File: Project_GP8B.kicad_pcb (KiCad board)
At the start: 4 copper layers, 133 x 93 mm, 96 parts, among them IC1 XC95288XL-10TQ144I, J1 Conn_01x05_Male, J2 TE_Eurocard_96pole, J3 5530843-2, J4 Conn_02x21_Odd_Even, U1 74AHC05, U10 74AHC1G04, U11 CD74AC238, U12 74AHC1G04, U13 CD74AC238, U14 74AHC08, U15 CD74AC238, U16 74AHC08, U17 74AHC138, U18 74HC165, U19 74AHCT244, U2 74AHC05, U20 74AHCT244, U21 74AHCT244, U22 74AHCT244, U23 74AHCT244, U24 74AHC273, U25 74AHCT595, U26 74AHC273, U27 74AHC273, U29 74AHC273, U3 74AHC1G04, U31 74AHC273, U33 74AHC273, U35 74AHC273, U36 74AHC1G04, U37 74AHC273, U38 74AHC374, U39 74AHC1G04, U4 74AHC1G04, U5 74AHC05, U6 74AHC273, U7 74AHCT273, U8 74HC163, U9 CD74AC238

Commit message: Adding license info on silks
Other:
- board text added: "Licensed under CERN OHL v.1.2"
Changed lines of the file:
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@@
   (general
     (thickness 1.6)
-    (drawings 29)
+    (drawings 30)
     (tracks 4985)
     (zones 0)
@@
     )
   )
+  (gr_text "Licensed under CERN OHL v.1.2" (at 170.3 122) (layer F.SilkS)
+    (effects (font (size 1 1) (thickness 0.15)))
+  )
   (gr_text "ALU - Unused pins" (at 108.5 114.5) (layer F.SilkS)

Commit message: Switching license to "CERN-OHLw v2 or later"
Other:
- board text added: "Licensed under CERN-OHL-W v2 or later"
- board text removed: "Licensed under CERN OHL v.1.2"

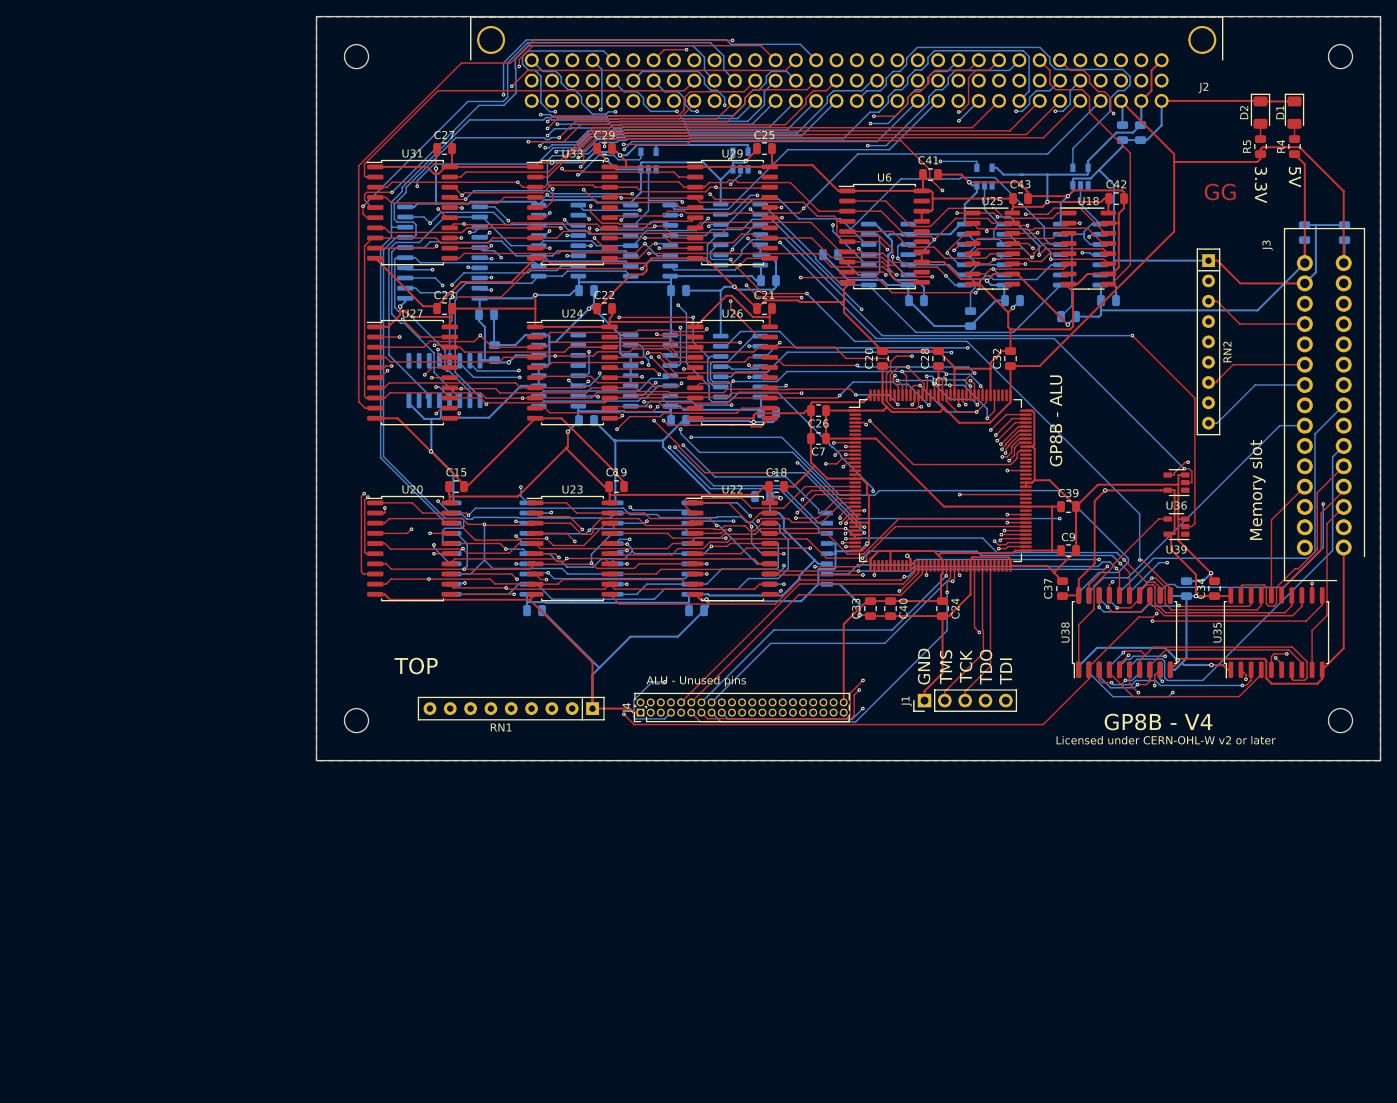
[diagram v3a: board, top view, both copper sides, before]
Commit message: Preparing footprint placement, removing old footprint
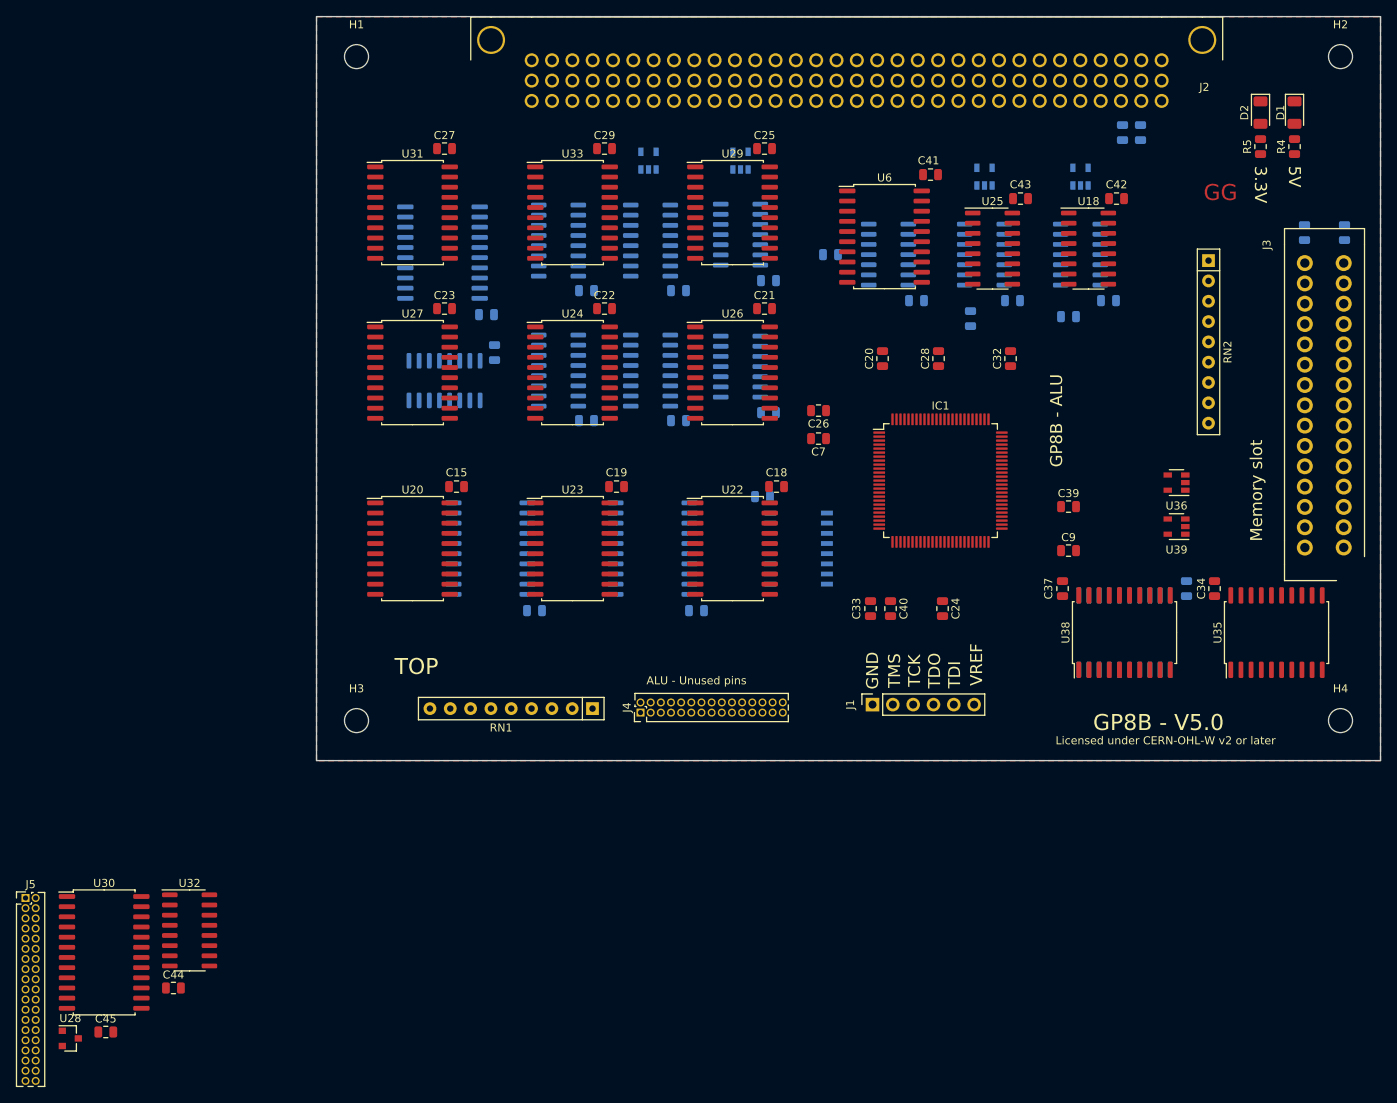
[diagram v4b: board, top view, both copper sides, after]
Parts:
- removed HOLE1, HOLE2, HOLE3, HOLE4: Hole_3mm, hole_3mm:Hole_3mm
- added C44: 10nF, Capacitor_SMD:C_0805_2012Metric, F.Cu at (43.1, 152.9)
- added C45: 10nF, Capacitor_SMD:C_0805_2012Metric, F.Cu at (34.7, 158.4)
- added H1: MountingHole_3mm, MountingHole:MountingHole_3mm, F.Cu at (66.0, 36.5)
- added H2: MountingHole_3mm, MountingHole:MountingHole_3mm, F.Cu at (189.0, 36.5)
- added H3: MountingHole_3mm, MountingHole:MountingHole_3mm, F.Cu at (66.0, 119.5)
- added H4: MountingHole_3mm, MountingHole:MountingHole_3mm, F.Cu at (189.0, 119.5)
- added J5: ALU_PINS, Connector_PinHeader_1.27mm:PinHeader_2x19_P1.27mm_Vertical, F.Cu at (24.6, 141.7)
- added U28: TPS7A0518PDBZR, Package_TO_SOT_SMD:SOT-23, F.Cu at (30.2, 159.2)
- added U30: SN74LVC8T245DW, Package_SO:SOIC-24W_7.5x15.4mm_P1.27mm, F.Cu at (34.5, 148.5)
- added U32: SN74AVC4T245D, Package_SO:SOIC-16_3.9x9.9mm_P1.27mm, F.Cu at (45.1, 145.7)
- C20, C24, C26, C28, C32, C39, C7, C9: value 10nF -> 100nF
- C33, C40: value 10nF -> 1uF
- IC1: value XC95288XL-10TQ144I -> XC2C256-VQ100; footprint Package_QFP:TQFP-144_20x20mm_P0.5mm -> Package_QFP:VQFP-100_14x14mm_P0.5mm
- J1: value Conn_01x05_Male -> ALU_JTAG; footprint Connector_PinHeader_2.54mm:PinHeader_1x05_P2.54mm_Vertical -> Connector_PinSocket_2.54mm:PinSocket_1x06_P2.54mm_Vertical
- J4: value Conn_02x21_Odd_Even -> UnusedPins_Connector; footprint Connector_PinHeader_1.27mm:PinHeader_2x21_P1.27mm_Vertical -> Connector_PinHeader_1.27mm:PinHeader_2x15_P1.27mm_Vertical
- moved J1 6.52 mm to (130.5, 117.5)
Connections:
- net /BCSPI_CLK renamed /BCFG_SPI_CLK
- net /Connecteur/BDATASRC_0 renamed /Connector/BDATASRC_0
- net /Connecteur/BDATASRC_1 renamed /Connector/BDATASRC_1
- net /Connecteur/BDATASRC_2 renamed /Connector/BDATASRC_2
- net /Connecteur/BDATASRC_3 renamed /Connector/BDATASRC_3
- net /Connecteur/BDATASRC_4 renamed /Connector/BDATASRC_4
- net /Connecteur/BDATASRC_5 renamed /Connector/BDATASRC_5
- net /Connecteur/BDATASRC_6 renamed /Connector/BDATASRC_6
- net /Connecteur/BDATASRC_7 renamed /Connector/BDATASRC_7
- net /Connecteur/BJMPSRC_0 renamed /Connector/BJMPSRC_0
- net /Connecteur/BJMPSRC_1 renamed /Connector/BJMPSRC_1
- net /Connecteur/BJMPSRC_10 renamed /Connector/BJMPSRC_10
- net /Connecteur/BJMPSRC_11 renamed /Connector/BJMPSRC_11
- net /Connecteur/BJMPSRC_12 renamed /Connector/BJMPSRC_12
- net /Connecteur/BJMPSRC_13 renamed /Connector/BJMPSRC_13
- net /Connecteur/BJMPSRC_14 renamed /Connector/BJMPSRC_14
- net /Connecteur/BJMPSRC_15 renamed /Connector/BJMPSRC_15
- net /Connecteur/BJMPSRC_16 renamed /Connector/BJMPSRC_16
- net /Connecteur/BJMPSRC_17 renamed /Connector/BJMPSRC_17
- net /Connecteur/BJMPSRC_18 renamed /Connector/BJMPSRC_18
- net /Connecteur/BJMPSRC_19 renamed /Connector/BJMPSRC_19
- net /Connecteur/BJMPSRC_2 renamed /Connector/BJMPSRC_2
- net /Connecteur/BJMPSRC_20 renamed /Connector/BJMPSRC_20
- net /Connecteur/BJMPSRC_21 renamed /Connector/BJMPSRC_21
- net /Connecteur/BJMPSRC_22 renamed /Connector/BJMPSRC_22
- net /Connecteur/BJMPSRC_23 renamed /Connector/BJMPSRC_23
- net /Connecteur/BJMPSRC_3 renamed /Connector/BJMPSRC_3
- net /Connecteur/BJMPSRC_4 renamed /Connector/BJMPSRC_4
- net /Connecteur/BJMPSRC_5 renamed /Connector/BJMPSRC_5
- net /Connecteur/BJMPSRC_6 renamed /Connector/BJMPSRC_6
- net /Connecteur/BJMPSRC_7 renamed /Connector/BJMPSRC_7
- net /Connecteur/BJMPSRC_8 renamed /Connector/BJMPSRC_8
- net /Connecteur/BJMPSRC_9 renamed /Connector/BJMPSRC_9
- net /Connecteur/BPCS_0 renamed /Connector/BPCS_0
- net /Connecteur/BPCS_1 renamed /Connector/BPCS_1
- net /Connecteur/BPCS_2 renamed /Connector/BPCS_2
- net /Connecteur/BPCS_3 renamed /Connector/BPCS_3
- net /Connecteur/BPCS_4 renamed /Connector/BPCS_4
- net /Connecteur/BPCS_5 renamed /Connector/BPCS_5
- net /Connecteur/BREAD1_0 renamed /Connector/BREAD1_0
- net /Connecteur/BREAD1_1 renamed /Connector/BREAD1_1
- net /Connecteur/BREAD1_2 renamed /Connector/BREAD1_2
- net /Connecteur/BREAD1_3 renamed /Connector/BREAD1_3
- net /Connecteur/BREAD1_4 renamed /Connector/BREAD1_4
- net /Connecteur/BREAD1_5 renamed /Connector/BREAD1_5
- net /Connecteur/BREAD1_6 renamed /Connector/BREAD1_6
- net /Connecteur/BREAD1_7 renamed /Connector/BREAD1_7
- net /Connecteur/BREAD2_0 renamed /Connector/BREAD2_0
- net /Connecteur/BREAD2_1 renamed /Connector/BREAD2_1
- net /Connecteur/BREAD2_2 renamed /Connector/BREAD2_2
- net /Connecteur/BREAD2_3 renamed /Connector/BREAD2_3
- net /Connecteur/BREAD2_4 renamed /Connector/BREAD2_4
- net /Connecteur/BREAD2_5 renamed /Connector/BREAD2_5
- net /Connecteur/BREAD2_6 renamed /Connector/BREAD2_6
- net /Connecteur/BREAD2_7 renamed /Connector/BREAD2_7
- net /Connecteur/BWRITE1_0 renamed /Connector/BWRITE1_0
- net /Connecteur/BWRITE1_1 renamed /Connector/BWRITE1_1
- net /Connecteur/BWRITE1_2 renamed /Connector/BWRITE1_2
- net /Connecteur/BWRITE1_3 renamed /Connector/BWRITE1_3
- net /Connecteur/BWRITE1_4 renamed /Connector/BWRITE1_4
- net /Connecteur/BWRITE1_5 renamed /Connector/BWRITE1_5
- net /Connecteur/BWRITE1_6 renamed /Connector/BWRITE1_6
- net /Connecteur/BWRITE1_7 renamed /Connector/BWRITE1_7
- net /Connecteur/BWRITE2_0 renamed /Connector/BWRITE2_0
- net /Connecteur/BWRITE2_1 renamed /Connector/BWRITE2_1
- net /Connecteur/BWRITE2_2 renamed /Connector/BWRITE2_2
- net /Connecteur/BWRITE2_3 renamed /Connector/BWRITE2_3
- net /Connecteur/BWRITE2_4 renamed /Connector/BWRITE2_4
- net /Connecteur/BWRITE2_5 renamed /Connector/BWRITE2_5
- net /Connecteur/BWRITE2_6 renamed /Connector/BWRITE2_6
- net /Connecteur/BWRITE2_7 renamed /Connector/BWRITE2_7
- C24 pad 1: +3V3 -> +1V8
- C28 pad 1: +3V3 -> +1V8
- C40 pad 1: +3V3 -> +1V8
- IC1 pad 1: +3V3 -> /NumberSelect/BOPRESULT_4
- IC1 pad 10: /Operation/UNUSED_A0 -> /Operation/DLEFT_4
- IC1 pad 100: /Operation/UNUSED_C7 -> GND
- IC1 pad 11: /Operation/UNUSED_A1 -> /Operation/DLEFT_5
- IC1 pad 12: /Operation/UNUSED_A2 -> /Operation/DLEFT_6
- IC1 pad 13: /Operation/UNUSED_A3 -> /Operation/DLEFT_7
- IC1 pad 14: /NumberSelect/BOPRESULT_5 -> Net-(IC1-Pad14)
- IC1 pad 18: GND -> Net-(IC1-Pad18)
- IC1 pad 19: Net-(IC1-Pad19) -> /NumberSelect/BOPRESULT_7
- IC1 pad 2: Net-(IC1-Pad2) -> /Operation/UNUSED_D2
- IC1 pad 20: /NumberSelect/BOPRESULT_0 -> +3V3
- IC1 pad 21: /Operation/UNUSED_A4 -> GND
- IC1 pad 22: /Operation/UNUSED_A5 -> /Operation/CPLD_OPCHOOSE_CLK
- IC1 pad 23: /Operation/UNUSED_A6 -> /Operation/CPLD_OPRIGHT_CLK
- IC1 pad 24: /Operation/UNUSED_A7 -> /NumberSelect/BOPRESULT_6
- IC1 pad 25: /Operation/UNUSED_E0 -> GND
- IC1 pad 26: /Operation/UNUSED_E1 -> +1V8
- IC1 pad 27: /Operation/UNUSED_E2 -> /Operation/CPLD_OPLEFT_CLK
- IC1 pad 28: /Operation/UNUSED_E3 -> /Operation/UNUSED_D3
- IC1 pad 29: GND -> /Operation/DLEFT_0
- IC1 pad 3: Net-(IC1-Pad3) -> /Operation/UNUSED_D1
- IC1 pad 30: /OPLEFT_CLK -> /Operation/DLEFT_1
- IC1 pad 31: /Operation/UNUSED_E4 -> GND
- IC1 pad 32: /OPRIGHT_CLK -> /Operation/DLEFT_2
- IC1 pad 33: /Operation/UNUSED_E5 -> /Operation/DLEFT_3
- IC1 pad 34: /Operation/UNUSED_E6 -> /Operation/DLEFT_4
- IC1 pad 35: /Operation/UNUSED_E7 -> /Operation/DLEFT_5
- IC1 pad 36: GND -> /Operation/DLEFT_6
- IC1 pad 37: +3V3 -> /Operation/DLEFT_7
- IC1 pad 38: /OPC_CLK -> +3V3
- IC1 pad 4: /NumberSelect/BOPRESULT_7 -> /Operation/UNUSED_D0
- IC1 pad 40: Net-(IC1-Pad40) -> /Operation/UNUSED_C0
- IC1 pad 41: Net-(IC1-Pad41) -> /Operation/UNUSED_C1
- IC1 pad 42: +3V3 -> /Operation/UNUSED_C2
- IC1 pad 43: Net-(IC1-Pad43) -> /Operation/UNUSED_C3
- IC1 pad 44: Net-(IC1-Pad44) -> /Operation/UNUSED_C4
- IC1 pad 45: Net-(IC1-Pad45) -> /Operation/TDI
- IC1 pad 46: Net-(IC1-Pad46) -> /Operation/UNUSED_C5
- IC1 pad 47: GND -> /Operation/TMS
- IC1 pad 48: /Operation/UNUSED_B0 -> /Operation/TCK
- IC1 pad 49: /Operation/UNUSED_B1 -> /Operation/UNUSED_C6
- IC1 pad 5: Net-(IC1-Pad5) -> +3V3
- IC1 pad 50: /Operation/UNUSED_B2 -> /Operation/UNUSED_C7
- IC1 pad 51: /Operation/UNUSED_B3 -> +3V3
- IC1 pad 52: Net-(IC1-Pad52) -> /Operation/UNUSED_A0
- IC1 pad 53: Net-(IC1-Pad53) -> /Operation/UNUSED_A1
- IC1 pad 54: Net-(IC1-Pad54) -> /Operation/UNUSED_A2
- IC1 pad 55: +3V3 -> /Operation/UNUSED_A3
- IC1 pad 56: /Operation/UNUSED_B4 -> /Operation/UNUSED_A4
- IC1 pad 57: /Operation/UNUSED_B5 -> +1V8
- IC1 pad 58: /Operation/UNUSED_B6 -> /Operation/UNUSED_A5
- IC1 pad 59: /Operation/UNUSED_B7 -> /Operation/UNUSED_A6
- IC1 pad 6: Net-(IC1-Pad6) -> /Operation/DLEFT_0
- IC1 pad 60: Net-(IC1-Pad60) -> /Operation/UNUSED_A7
- IC1 pad 63: /Operation/TDI -> Net-(IC1-Pad63)
- IC1 pad 65: /Operation/TMS -> Net-(IC1-Pad65)
- IC1 pad 66: Net-(IC1-Pad66) -> /Operation/UNUSED_B0
- IC1 pad 67: /Operation/TCK -> /Operation/UNUSED_B1
- IC1 pad 68: Net-(IC1-Pad68) -> /Operation/UNUSED_B2
- IC1 pad 69: Net-(IC1-Pad69) -> GND
- IC1 pad 7: Net-(IC1-Pad7) -> /Operation/DLEFT_1
- IC1 pad 70: Net-(IC1-Pad70) -> /Operation/UNUSED_B3
- IC1 pad 71: Net-(IC1-Pad71) -> /Operation/UNUSED_B4
- IC1 pad 72: GND -> /Operation/UNUSED_B5
- IC1 pad 73: +3V3 -> /Operation/UNUSED_B6
- IC1 pad 74: /Operation/UNUSED_D7 -> /Operation/UNUSED_B7
- IC1 pad 75: /Operation/UNUSED_D6 -> GND
- IC1 pad 76: /Operation/UNUSED_D5 -> Net-(IC1-Pad76)
- IC1 pad 77: /Operation/UNUSED_D4 -> /NumberSelect/BOPRESULT_3
- IC1 pad 78: /Operation/UNUSED_D3 -> /NumberSelect/BOPRESULT_1
- IC1 pad 79: /Operation/UNUSED_D2 -> /Operation/DLEFT_0
- IC1 pad 8: +3V3 -> /Operation/DLEFT_2
- IC1 pad 80: /Operation/UNUSED_D1 -> /Operation/DLEFT_1
- IC1 pad 81: /NumberSelect/BOPRESULT_4 -> /Operation/DLEFT_2
- IC1 pad 82: /Operation/UNUSED_D0 -> /Operation/DLEFT_3
- IC1 pad 83: Net-(IC1-Pad83) -> /Operation/TDO
- IC1 pad 84: +3V3 -> GND
- IC1 pad 85: Net-(IC1-Pad85) -> /Operation/DLEFT_4
- IC1 pad 86: Net-(IC1-Pad86) -> /Operation/DLEFT_5
- IC1 pad 87: /NumberSelect/BOPRESULT_6 -> /Operation/DLEFT_6
- IC1 pad 88: Net-(IC1-Pad88) -> +3V3
- IC1 pad 89: GND -> /Operation/DLEFT_7
- IC1 pad 9: /NumberSelect/BOPRESULT_1 -> /Operation/DLEFT_3
- IC1 pad 90: GND -> Net-(IC1-Pad90)
- IC1 pad 93: /NumberSelect/BOPRESULT_2 -> /NumberSelect/BOPRESULT_5
- IC1 pad 97: Net-(IC1-Pad97) -> /NumberSelect/BOPRESULT_2
- IC1 pad 98: /NumberSelect/BOPRESULT_3 -> +3V3
- IC1 pad 99: GND -> /NumberSelect/BOPRESULT_0
- J4 pad 30: /Operation/UNUSED_D4 -> +3V3
- U11 pad 10: /OPC_CLK -> /OPCHOOSE_CLK
- U18 pad 11: /NUMBER_0 -> /SPI/BUFF_0
- U18 pad 12: /NUMBER_1 -> /SPI/BUFF_1
- U18 pad 13: /NUMBER_2 -> /SPI/BUFF_2
- U18 pad 14: /NUMBER_3 -> /SPI/BUFF_3
- U6 pad 12: Net-(U6-Pad12) -> /SPI/BUFF_0
- U6 pad 13: +5V -> /NUMBER_4
- U6 pad 14: +5V -> /NUMBER_5
- U6 pad 15: Net-(U6-Pad15) -> /SPI/BUFF_1
- U6 pad 16: Net-(U6-Pad16) -> /SPI/BUFF_2
- U6 pad 17: +5V -> /NUMBER_6
- U6 pad 18: +5V -> /NUMBER_7
- U6 pad 19: Net-(U6-Pad19) -> /SPI/BUFF_3
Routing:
- net GND: track 940.8 -> 0.00 mm, vias 17 -> 0
- net +5V: track 682.7 -> 0.00 mm, vias 13 -> 0
- net /NUMBER_2: track 420.7 -> 0.00 mm, vias 11 -> 0
- net /NUMBER_1: track 411.9 -> 0.00 mm, vias 13 -> 0
- net /NUMBER_3: track 402.2 -> 0.00 mm, vias 13 -> 0
- net /NUMBER_0: track 400.6 -> 0.00 mm, vias 12 -> 0
- net /NUMBER_4: track 372.0 -> 0.00 mm, vias 11 -> 0
- net /NUMBER_6: track 354.5 -> 0.00 mm, vias 13 -> 0
- net /NUMBER_7: track 354.1 -> 0.00 mm, vias 11 -> 0
- net /NUMBER_5: track 343.3 -> 0.00 mm, vias 11 -> 0
- net +3V3: track 227.1 -> 0.00 mm
- net /NumberSelect/RAMDATA_3: track 194.6 -> 0.00 mm, vias 2 -> 0
- net /NumberSelect/RAMDATA_1: track 185.1 -> 0.00 mm, vias 2 -> 0
- net /RAM_OE_CONTROL: track 168.8 -> 0.00 mm, vias 3 -> 0
- net /NumberSelect/RAMDATA_2: track 156.4 -> 0.00 mm, vias 2 -> 0
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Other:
- board text added: "GP8B - V5.0"
- board text added: "VREF"
- board text removed: "GP8B - V4"

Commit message: Footprints placement
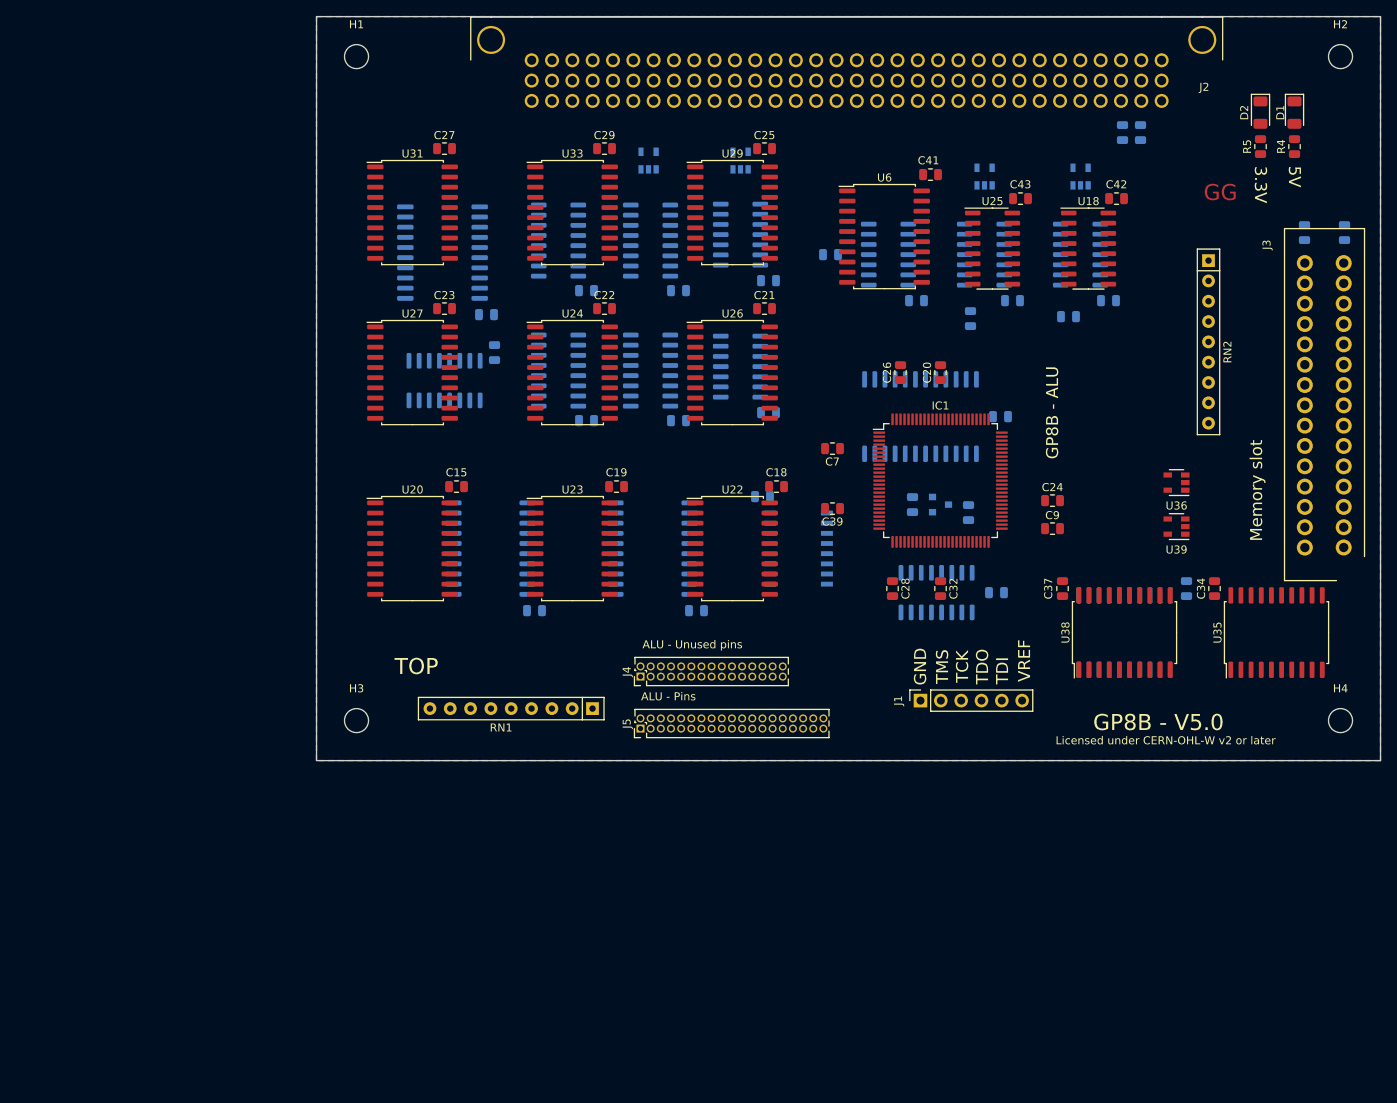
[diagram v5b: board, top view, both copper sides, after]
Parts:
- C33, C40, C44, C45, U28, U30, U32: moved to B.Cu
- moved C45 135.7 mm to (146.5, 81.5), turned to 180 degrees
- moved U28 127.6 mm to (139.0, 92.5)
- moved U30 122.1 mm to (136.5, 81.5), turned to 90 degrees
- moved C44 114.1 mm to (146.0, 103.5), turned to 180 degrees
- moved U32 102.5 mm to (138.5, 103.5), turned to 90 degrees
- moved J5 79.7 mm to (101.5, 120.5), turned to 90 degrees
- moved C32 30.1 mm to (139.0, 103.0), turned to 270 degrees
- moved C39 29.5 mm to (125.5, 93.0), turned to 180 degrees
- moved C28 29.3 mm to (133.0, 103.0), turned to 270 degrees
- moved C24 19.3 mm to (153.0, 92.0), turned to 0 degrees
- moved C33 17.1 mm to (142.5, 93.5)
- moved C40 13.3 mm to (135.5, 92.5)
- moved C26 11.3 mm to (134.0, 76.0), turned to 90 degrees
- moved C20 7.46 mm to (139.0, 76.0)
- moved J1 6.02 mm to (136.5, 117.0)
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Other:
- board text added: "ALU - Pins"

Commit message: Finishing the new PCB
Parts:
- added G***: LOGO, QRCode:QRCode, B.Cu at (156.8, 80.9)
- moved J1 1.58 mm to (135.0, 117.5)
- moved C24 0.50 mm to (153.0, 92.5)
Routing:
- net +5V: track 0.00 -> 660.9 mm, vias 0 -> 13
- net /NUMBER_1: track 0.00 -> 434.3 mm, vias 0 -> 8
- net /NUMBER_3: track 0.00 -> 423.6 mm, vias 0 -> 8
- net /NUMBER_7: track 0.00 -> 413.6 mm, vias 0 -> 12
- net GND: track 0.00 -> 410.5 mm, vias 0 -> 20
- net /NUMBER_0: track 0.00 -> 407.5 mm, vias 0 -> 11
- net /NUMBER_4: track 0.00 -> 397.7 mm, vias 0 -> 9
- net /NUMBER_6: track 0.00 -> 388.8 mm, vias 0 -> 11
- net /NUMBER_2: track 0.00 -> 386.9 mm, vias 0 -> 7
- net /NUMBER_5: track 0.00 -> 384.4 mm, vias 0 -> 13
- net +3V3: track 0.00 -> 238.9 mm, vias 0 -> 3
- net /BRAMADD1_CLK: track 0.00 -> 184.9 mm, vias 0 -> 2
- net /NumberSelect/RAMDATA_1: track 0.00 -> 182.7 mm, vias 0 -> 3
- net /NumberSelect/RAMDATA_3: track 0.00 -> 175.6 mm, vias 0 -> 2
- net /NumberSelect/RAMDATA_0: track 0.00 -> 160.5 mm, vias 0 -> 3
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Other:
- board text added: "SPS1"
